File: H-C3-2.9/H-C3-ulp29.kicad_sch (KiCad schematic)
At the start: 55 parts, among them J1 USB_C_Receptacle_USB2.0, J2 AFC24-S24FIC-00, J4 SM04B-SRSS-TB_LF__SN_, Q1 Si1308, Q2 Si2301CDS, SW1 K2-1806SQ-A2DW-04, SW2 K2-1806SQ-A2DW-04, SW3 K2-1806SQ-A2DW-04, U1 E104-BT5032A, U2 XC6206PxxxMR, U3 CH340C, U8 PCF8563T, Y1 Crystal_Small

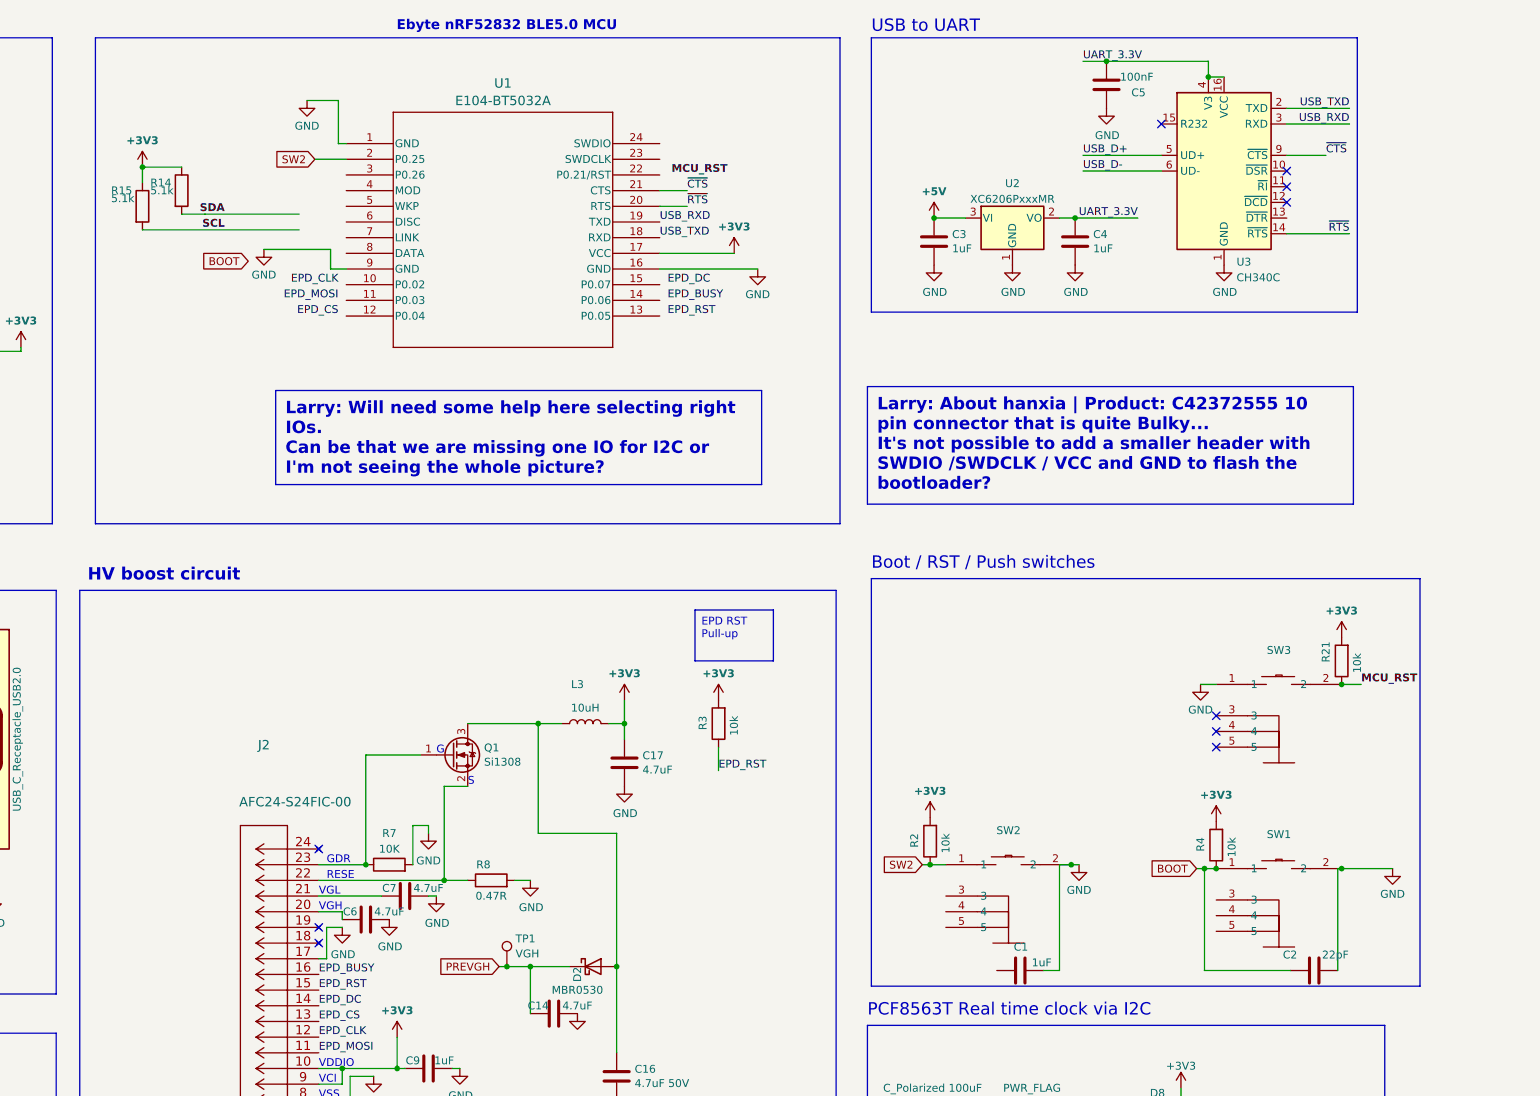
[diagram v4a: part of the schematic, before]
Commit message: Final decision about MCU
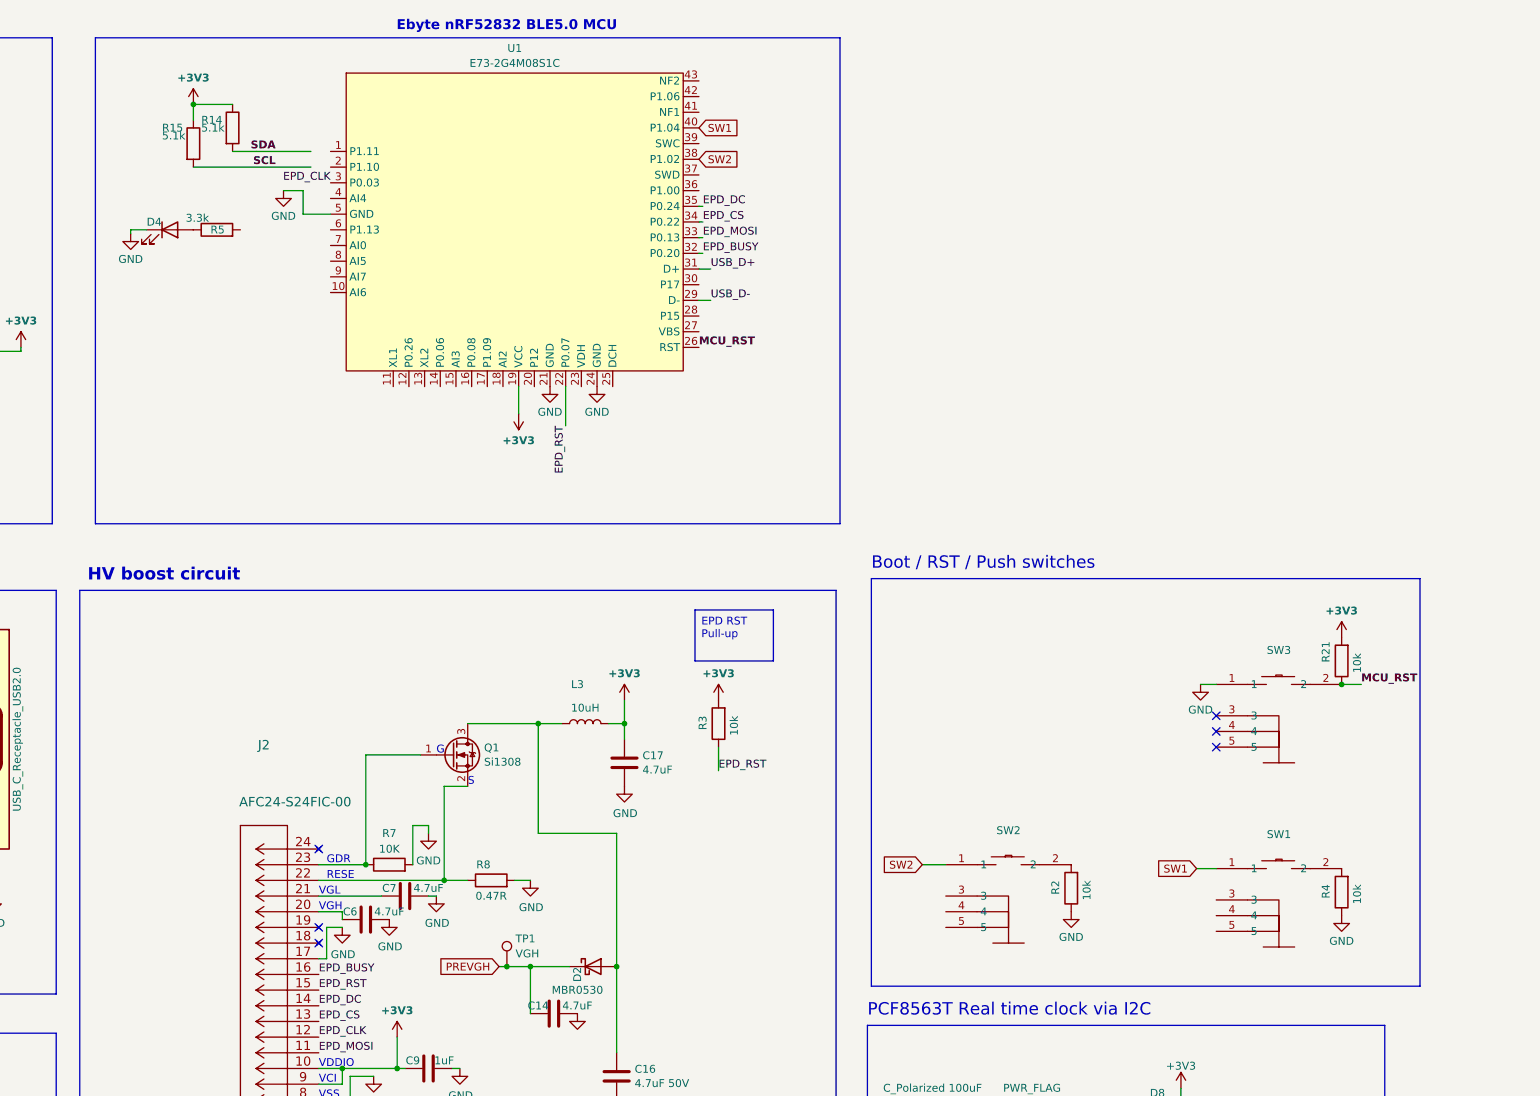
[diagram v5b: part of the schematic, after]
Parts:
- removed C1: 1uF, Capacitor_SMD:C_0402_1005Metric, symbol Device:C
- removed C2: 22pF, Capacitor_SMD:C_0402_1005Metric, symbol Device:C
- removed C3, C4: 1uF, Capacitor_SMD:C_0805_2012Metric, symbol Device:C
- removed C5: 100nF, Capacitor_SMD:C_0805_2012Metric, symbol Device:C
- removed U1: E104-BT5032A, footprints:nRF52832_E104-BT5032A_BYT, symbol Nordic:E104-BT5032A
- removed U2: XC6206PxxxMR, Package_TO_SOT_SMD:SOT-23-3, symbol Regulator_Linear:XC6206PxxxMR
- removed U3: CH340C, Package_SO:SOIC-16_3.9x9.9mm_P1.27mm, symbol Interface_USB:CH340C
- added D4: LED, LED_SMD:LED_0402_1005Metric, symbol Device:LED
- added R5: 3.3k, Resistor_SMD:R_0402_1005Metric, symbol Device:R
- added U1: E73-2G4M08S1C, footprints:C356849-nRF52840, symbol easyeda:E73-2G4M08S1C
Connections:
- net +3V3: now also U1.19 (VCC); no longer R2.2, R4.2
- net EPD_BUSY: now also U1.32 (P0.20)
- net EPD_CLK: now also U1.3 (P0.03)
- net EPD_CS: now also U1.34 (P0.22)
- net EPD_DC: now also U1.35 (P0.24)
- net EPD_MOSI: now also U1.33 (P0.13)
- net EPD_RST: now also U1.22 (P0.07)
- net GND: now also R2.1, R4.1, D4.1 (K), U1.21 (GND), U1.24 (GND), U1.5 (GND); no longer SW1.2, SW2.2
- net MCU_RST: now also U1.26 (RST)
- net SW2: now also U1.38 (P1.02); no longer R2.1
- net USB_D+: now also U1.31 (D+)
- net USB_D-: now also U1.29 (D-)
- net BOOT renamed SW1
- net SW1: now also U1.40 (P1.04); no longer R4.1
- new net: D4.2 (A), R5.1
- new net: R2.2, SW2.2
- new net: R4.2, SW1.2
- no-connect marks 13 -> 9
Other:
- note removed: "USB to UART"
- moved on the sheet: R14, R15

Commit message: Starting to test routing posibilities
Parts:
- added R6: 10k, Resistor_SMD:R_0402_1005Metric, symbol Device:R
- added SW4: K2-1806SQ-A2DW-04, footprints:KEY-SMD_K2-1806SQ-A3DW-04, symbol easyeda:K2-1806SQ-A2DW-04
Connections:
- net +3V3: now also R6.2
- net EPD_BUSY: now also U1.35 (P0.24); no longer U1.32 (P0.20)
- net EPD_CLK: now also U1.22 (P0.07); no longer U1.3 (P0.03)
- net EPD_CS: now also U1.16 (P0.08); no longer U1.34 (P0.22)
- net EPD_DC: now also U1.34 (P0.22); no longer U1.35 (P0.24)
- net EPD_MOSI: now also U1.17 (P1.09); no longer U1.33 (P0.13)
- net EPD_RST: now also U1.3 (P0.03); no longer U1.22 (P0.07)
- net GND: now also SW4.1
- net SCL: now also U1.2 (P1.10)
- net SDA: now also U1.1 (P1.11)
- net at R5.2: now also U1.6 (P1.13)
- new net MCU_BOOT: R6.1, SW4.2, U1.33 (P0.13)
- no-connect marks 9 -> 12
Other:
- moved on the sheet: D4, R14, R15, R5

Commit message: Please approve routing
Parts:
- removed R6: 10k, Resistor_SMD:R_0402_1005Metric, symbol Device:R
- removed SW4: K2-1806SQ-A2DW-04, footprints:KEY-SMD_K2-1806SQ-A3DW-04, symbol easyeda:K2-1806SQ-A2DW-04
- added C1, C2: 10uF, Capacitor_SMD:C_0805_2012Metric, symbol Device:C
- added CN1: HX JN1.27-2X5 TP H4.9, footprints:C42372555-SWD_10P-P1.27, symbol easyeda:HXJN1.27-2X5TPH4.9
- added U2: MCP1700-3302E_SOT23, Package_TO_SOT_SMD:SOT-23, symbol epaper-breakout-rescue:MCP1700-3302E_SOT23-Regulator_Linear
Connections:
- net +3V3: now also C2.2, CN1.2, U2.2 (VO); no longer D5.1 (K), Q2.2 (S)
- net EPD_DC: now also U1.14 (P0.06); no longer U1.34 (P0.22)
- net GND: now also C1.1, C2.1, CN1.10, CN1.4, CN1.6, CN1.8, U2.1 (GND)
- net MCU_RST: now also CN1.9
- net SWDIO: now reaches U1.37 (SWD)
- net SWDIO: now also CN1.1
- net SWCLK: now reaches U1.39 (SWC)
- net SWCLK: now also CN1.3
- net MCU_BOOT: no longer names the net of U1.33 (P0.13)
- new net +VIN: C1.2, D5.1 (K), Q2.2 (S), U2.3 (VI)
- new net SWO ??: CN1.5
- no-connect marks 12 -> 10
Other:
- note added: "CR2450 and power switching + LDO"
- note added: "Power 3.3V"
- note added: "Reset / Push switches"
- note added: "SWD DEBUGGER"
- note removed: "Boot / RST / Push switches"
- note removed: "CR2450 and power management"
- moved on the sheet: BT1, D5, Q2, R10
